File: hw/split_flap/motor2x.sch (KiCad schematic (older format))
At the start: 5 parts, among them J10 Conn_01x05, J9 Conn_01x05, U4 ULN2803A, U9 74HC595

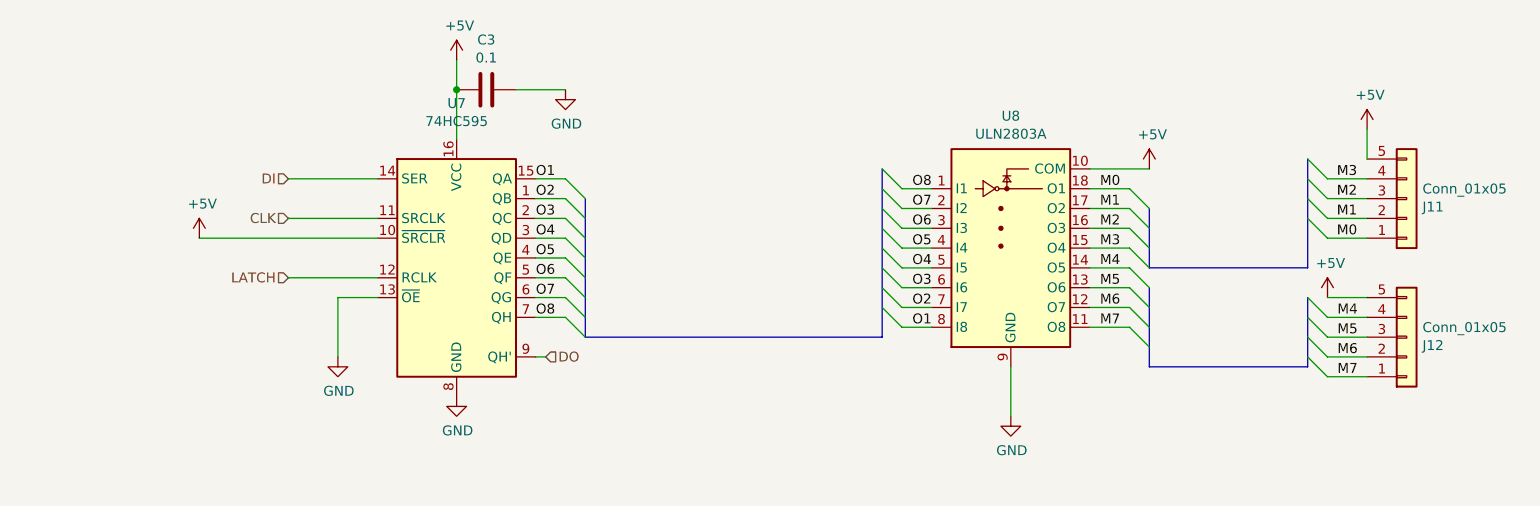
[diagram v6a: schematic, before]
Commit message: Add VCC for motors
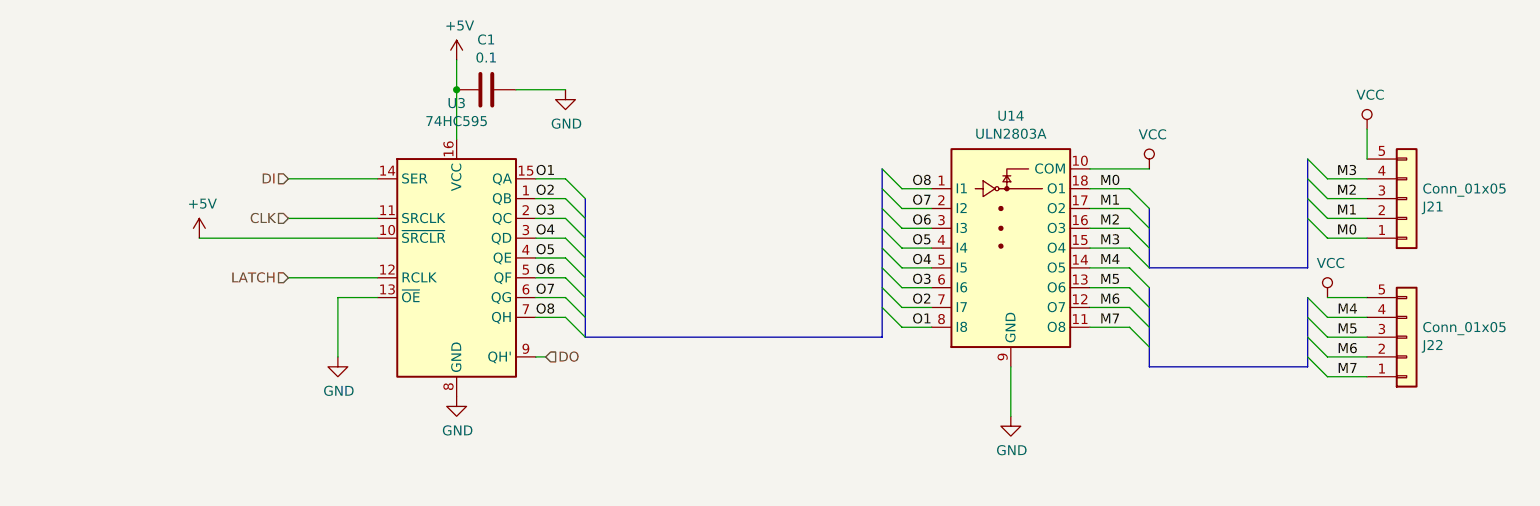
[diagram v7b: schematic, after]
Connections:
- net +5V: no longer J10.5 (Pin_5), J9.5 (Pin_5), U4.10 (COM)
- new net VCC: J10.5 (Pin_5), J9.5 (Pin_5), U4.10 (COM)
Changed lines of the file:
@@
 $Descr A4 11693 8268
 encoding utf-8
-Sheet 5 6
+Sheet 2 6
 Title ""
 Date ""
@@
 AR Path="/5E0964A4/5E0DEDAF" Ref="#PWR033"  Part="1"
 AR Path="/5E0B21A0/5E0DEDAF" Ref="#PWR051"  Part="1"
-F 0 "#PWR042" H 4850 3850 50  0001 C CNN
+F 0 "#PWR0159" H 4850 3850 50  0001 C CNN
 F 1 "GND" H 4855 3927 50  0000 C CNN
 F 2 "" H 4850 4100 50  0001 C CNN
@@
 AR Path="/5E0964A4/5DF98B62" Ref="#PWR032"  Part="1"
 AR Path="/5E0B21A0/5DF98B62" Ref="#PWR050"  Part="1"
-F 0 "#PWR041" H 4850 2250 50  0001 C CNN
+F 0 "#PWR012" H 4850 2250 50  0001 C CNN
 F 1 "+5V" H 4865 2573 50  0000 C CNN
 F 2 "" H 4850 2400 50  0001 C CNN
@@
 AR Path="/5E0964A4/5DF9B643" Ref="#PWR031"  Part="1"
 AR Path="/5E0B21A0/5DF9B643" Ref="#PWR049"  Part="1"
-F 0 "#PWR040" H 4250 3650 50  0001 C CNN
+F 0 "#PWR011" H 4250 3650 50  0001 C CNN
 F 1 "GND" H 4255 3727 50  0000 C CNN
 F 2 "" H 4250 3900 50  0001 C CNN
@@
 AR Path="/5E0964A4/5DF9D02C" Ref="#PWR030"  Part="1"
 AR Path="/5E0B21A0/5DF9D02C" Ref="#PWR048"  Part="1"
-F 0 "#PWR039" H 3550 3150 50  0001 C CNN
+F 0 "#PWR08" H 3550 3150 50  0001 C CNN
 F 1 "+5V" H 3565 3473 50  0000 C CNN
 F 2 "" H 3550 3300 50  0001 C CNN
@@
 AR Path="/5E092C79/5E0E710C" Ref="C3"  Part="1"
 AR Path="/5E0B21A0/5E0E710C" Ref="C4"  Part="1"
-F 0 "C3" V 5252 2550 50  0000 C CNN
+F 0 "C1" V 5252 2550 50  0000 C CNN
 F 1 "0.1" V 5161 2550 50  0000 C CNN
 F 2 "Capacitor_THT:C_Disc_D4.3mm_W1.9mm_P5.00mm" H 5038 2400 50  0001 C CNN
@@
 AR Path="/5E0964A4/5E0E7881" Ref="#PWR034"  Part="1"
 AR Path="/5E0B21A0/5E0E7881" Ref="#PWR052"  Part="1"
-F 0 "#PWR043" H 5400 2300 50  0001 C CNN
+F 0 "#PWR013" H 5400 2300 50  0001 C CNN
 F 1 "GND" H 5405 2377 50  0000 C CNN
 F 2 "" H 5400 2550 50  0001 C CNN
@@
 AR Path="/5E0964A4/5DF4397F" Ref="U5"  Part="1"
 AR Path="/5E092C79/5DF4397F" Ref="U7"  Part="1"
-F 0 "U7" H 4850 4181 50  0000 C CNN
+F 0 "U3" H 4850 4181 50  0000 C CNN
 F 1 "74HC595" H 4850 4090 50  0000 C CNN
 F 2 "Package_SO:SOP-16_4.55x10.3mm_P1.27mm" H 4850 3400 50  0001 C CNN
@@
 Wire Wire Line
 	5250 3700 5400 3700
-$Comp
-L power:+5V #PWR?
-U 1 1 5E0DED8E
-P 9250 3600
-AR Path="/5E0DED8E" Ref="#PWR?"  Part="1"
-AR Path="/5E0CA2EA/5E0DED8E" Ref="#PWR0122"  Part="1"
-AR Path="/5E1C4151/5E0DED8E" Ref="#PWR0128"  Part="1"
-AR Path="/5E1CE3D2/5E0DED8E" Ref="#PWR0134"  Part="1"
-AR Path="/5E1D4C2D/5E0DED8E" Ref="#PWR0140"  Part="1"
-AR Path="/5E2ED868/5E0DED8E" Ref="#PWR019"  Part="1"
-AR Path="/5DEBFEF8/5E0DED8E" Ref="#PWR0150"  Part="1"
-AR Path="/5DED9C19/5E0DED8E" Ref="#PWR0156"  Part="1"
-AR Path="/5DFFABAB/5E0DED8E" Ref="#PWR?"  Part="1"
-AR Path="/5DFFD987/5E0DED8E" Ref="#PWR?"  Part="1"
-AR Path="/5E08C84E/5E0DED8E" Ref="#PWR?"  Part="1"
-AR Path="/5E08C85A/5E0DED8E" Ref="#PWR?"  Part="1"
-AR Path="/5E092C79/5E0DED8E" Ref="#PWR047"  Part="1"
-AR Path="/5E0964A4/5E0DED8E" Ref="#PWR038"  Part="1"
-AR Path="/5E0B21A0/5E0DED8E" Ref="#PWR056"  Part="1"
-F 0 "#PWR047" H 9250 3450 50  0001 C CNN
-F 1 "+5V" H 9265 3773 50  0000 C CNN
-F 2 "" H 9250 3600 50  0001 C CNN
-F 3 "" H 9250 3600 50  0001 C CNN
-	1    9250 3600
-	1    0    0    -1
-$EndComp
 $Comp
 L Connector_Generic:Conn_01x05 J?
@@
 AR Path="/5E0964A4/5E0DED94" Ref="J10"  Part="1"
 AR Path="/5E0B21A0/5E0DED94" Ref="J14"  Part="1"
-F 0 "J12" H 9730 3842 50  0000 L CNN
+F 0 "J22" H 9730 3842 50  0000 L CNN
 F 1 "Conn_01x05" H 9730 3751 50  0000 L CNN
 F 2 "Connector_JST:JST_XH_B5B-XH-A_1x05_P2.50mm_Vertical" H 9650 3800 50  0001 C CNN
@@
 	1    9650 3800
 	1    0    0    1
-$EndComp
-Wire Wire Line
-	9450 2750 9450 2900
-$Comp
-L power:+5V #PWR?
-U 1 1 5E0DED9D
-P 9450 2750
-AR Path="/5E0DED9D" Ref="#PWR?"  Part="1"
-AR Path="/5E0CA2EA/5E0DED9D" Ref="#PWR0123"  Part="1"
-AR Path="/5E1C4151/5E0DED9D" Ref="#PWR0129"  Part="1"
-AR Path="/5E1CE3D2/5E0DED9D" Ref="#PWR0135"  Part="1"
-AR Path="/5E1D4C2D/5E0DED9D" Ref="#PWR0141"  Part="1"
-AR Path="/5E2ED868/5E0DED9D" Ref="#PWR018"  Part="1"
-AR Path="/5DEBFEF8/5E0DED9D" Ref="#PWR0151"  Part="1"
-AR Path="/5DED9C19/5E0DED9D" Ref="#PWR0157"  Part="1"
-AR Path="/5DFFABAB/5E0DED9D" Ref="#PWR?"  Part="1"
-AR Path="/5DFFD987/5E0DED9D" Ref="#PWR?"  Part="1"
-AR Path="/5E08C84E/5E0DED9D" Ref="#PWR?"  Part="1"
-AR Path="/5E08C85A/5E0DED9D" Ref="#PWR?"  Part="1"
-AR Path="/5E092C79/5E0DED9D" Ref="#PWR046"  Part="1"
-AR Path="/5E0964A4/5E0DED9D" Ref="#PWR037"  Part="1"
-AR Path="/5E0B21A0/5E0DED9D" Ref="#PWR055"  Part="1"
-F 0 "#PWR046" H 9450 2600 50  0001 C CNN
-F 1 "+5V" H 9465 2923 50  0000 C CNN
-F 2 "" H 9450 2750 50  0001 C CNN
-F 3 "" H 9450 2750 50  0001 C CNN
-	1    9450 2750
-	1    0    0    -1
-$EndComp
-$Comp
-L power:+5V #PWR?
-U 1 1 5E0DEDA9
-P 8350 2950
-AR Path="/5E0DEDA9" Ref="#PWR?"  Part="1"
-AR Path="/5E0CA2EA/5E0DEDA9" Ref="#PWR0125"  Part="1"
-AR Path="/5E1C4151/5E0DEDA9" Ref="#PWR0131"  Part="1"
-AR Path="/5E1CE3D2/5E0DEDA9" Ref="#PWR0137"  Part="1"
-AR Path="/5E1D4C2D/5E0DEDA9" Ref="#PWR0143"  Part="1"
-AR Path="/5E2ED868/5E0DEDA9" Ref="#PWR017"  Part="1"
-AR Path="/5DEBFEF8/5E0DEDA9" Ref="#PWR0152"  Part="1"
-AR Path="/5DED9C19/5E0DEDA9" Ref="#PWR0158"  Part="1"
-AR Path="/5DFFABAB/5E0DEDA9" Ref="#PWR?"  Part="1"
-AR Path="/5DFFD987/5E0DEDA9" Ref="#PWR?"  Part="1"
-AR Path="/5E08C84E/5E0DEDA9" Ref="#PWR?"  Part="1"
-AR Path="/5E08C85A/5E0DEDA9" Ref="#PWR?"  Part="1"
-AR Path="/5E092C79/5E0DEDA9" Ref="#PWR045"  Part="1"
-AR Path="/5E0964A4/5E0DEDA9" Ref="#PWR036"  Part="1"
-AR Path="/5E0B21A0/5E0DEDA9" Ref="#PWR054"  Part="1"
-F 0 "#PWR045" H 8350 2800 50  0001 C CNN
-F 1 "+5V" H 8365 3123 50  0000 C CNN
-F 2 "" H 8350 2950 50  0001 C CNN
-F 3 "" H 8350 2950 50  0001 C CNN
-	1    8350 2950
-	1    0    0    -1
 $EndComp
 $Comp
@@
 AR Path="/5E0964A4/5E0DEDB5" Ref="#PWR035"  Part="1"
 AR Path="/5E0B21A0/5E0DEDB5" Ref="#PWR053"  Part="1"
-F 0 "#PWR044" H 7650 3950 50  0001 C CNN
+F 0 "#PWR0160" H 7650 3950 50  0001 C CNN
 F 1 "GND" H 7655 4027 50  0000 C CNN
 F 2 "" H 7650 4200 50  0001 C CNN
@@
 AR Path="/5E0964A4/5E0DEDBB" Ref="J9"  Part="1"
 AR Path="/5E0B21A0/5E0DEDBB" Ref="J13"  Part="1"
-F 0 "J11" H 9730 3142 50  0000 L CNN
+F 0 "J21" H 9730 3142 50  0000 L CNN
 F 1 "Conn_01x05" H 9730 3051 50  0000 L CNN
 F 2 "Connector_JST:JST_XH_B5B-XH-A_1x05_P2.50mm_Vertical" H 9650 3100 50  0001 C CNN
@@
 AR Path="/5E0964A4/5E0DEDCB" Ref="U6"  Part="1"
 AR Path="/5E0B21A0/5E0DEDCB" Ref="U10"  Part="1"
-F 0 "U8" H 7650 3817 50  0000 C CNN
+F 0 "U14" H 7650 3817 50  0000 C CNN
 F 1 "ULN2803A" H 7650 3726 50  0000 C CNN
 F 2 "Package_SO:SOP-18_7x12.5mm_P1.27mm" H 7700 2600 50  0001 L CNN
@@
 Wire Bus Line
 	8350 3450 9150 3450
+$Comp
+L power:VCC #PWR055
+U 1 1 5DF9DFD8
+P 8350 2950
+AR Path="/5E092C79/5DF9DFD8" Ref="#PWR055"  Part="1"
+AR Path="/5DED9C19/5DF9DFD8" Ref="#PWR045"  Part="1"
+AR Path="/5E0964A4/5DF9DFD8" Ref="#PWR047"  Part="1"
+AR Path="/5E0B21A0/5DF9DFD8" Ref="#PWR057"  Part="1"
+F 0 "#PWR045" H 8350 2800 50  0001 C CNN
+F 1 "VCC" H 8367 3123 50  0000 C CNN
+F 2 "" H 8350 2950 50  0001 C CNN
+F 3 "" H 8350 2950 50  0001 C CNN
+	1    8350 2950
+	1    0    0    -1
+$EndComp
+Wire Wire Line
+	9450 2750 9450 2900
+$Comp
+L power:VCC #PWR056
+U 1 1 5DF9E5BE
+P 9450 2750
+AR Path="/5E092C79/5DF9E5BE" Ref="#PWR056"  Part="1"
+AR Path="/5DED9C19/5DF9E5BE" Ref="#PWR046"  Part="1"
+AR Path="/5E0964A4/5DF9E5BE" Ref="#PWR054"  Part="1"
+AR Path="/5E0B21A0/5DF9E5BE" Ref="#PWR058"  Part="1"
+F 0 "#PWR046" H 9450 2600 50  0001 C CNN
+F 1 "VCC" H 9467 2923 50  0000 C CNN
+F 2 "" H 9450 2750 50  0001 C CNN
+F 3 "" H 9450 2750 50  0001 C CNN
+	1    9450 2750
+	1    0    0    -1
+$EndComp
+$Comp
+L power:VCC #PWR069
+U 1 1 5DFA3442
+P 9250 3600
+AR Path="/5E092C79/5DFA3442" Ref="#PWR069"  Part="1"
+AR Path="/5DED9C19/5DFA3442" Ref="#PWR059"  Part="1"
+AR Path="/5E0964A4/5DFA3442" Ref="#PWR068"  Part="1"
+AR Path="/5E0B21A0/5DFA3442" Ref="#PWR070"  Part="1"
+F 0 "#PWR059" H 9250 3450 50  0001 C CNN
+F 1 "VCC" H 9267 3773 50  0000 C CNN
+F 2 "" H 9250 3600 50  0001 C CNN
+F 3 "" H 9250 3600 50  0001 C CNN
+	1    9250 3600
+	1    0    0    -1
+$EndComp
 Wire Bus Line
 	8350 3150 8350 3450

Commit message: Add mounting holes, logo and capacitor for +5V
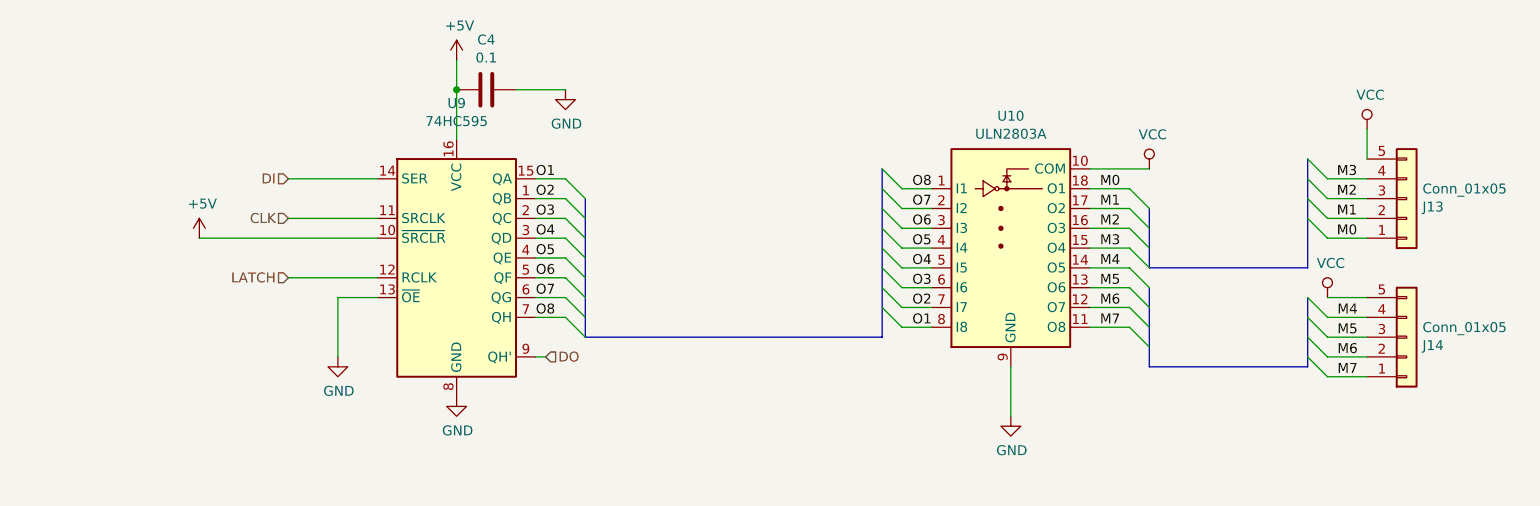
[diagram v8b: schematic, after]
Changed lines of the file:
@@
 AR Path="/5E0964A4/5E0DEDAF" Ref="#PWR033"  Part="1"
 AR Path="/5E0B21A0/5E0DEDAF" Ref="#PWR051"  Part="1"
-F 0 "#PWR0159" H 4850 3850 50  0001 C CNN
+F 0 "#PWR051" H 4850 3850 50  0001 C CNN
 F 1 "GND" H 4855 3927 50  0000 C CNN
 F 2 "" H 4850 4100 50  0001 C CNN
@@
 AR Path="/5E0964A4/5DF98B62" Ref="#PWR032"  Part="1"
 AR Path="/5E0B21A0/5DF98B62" Ref="#PWR050"  Part="1"
-F 0 "#PWR012" H 4850 2250 50  0001 C CNN
+F 0 "#PWR050" H 4850 2250 50  0001 C CNN
 F 1 "+5V" H 4865 2573 50  0000 C CNN
 F 2 "" H 4850 2400 50  0001 C CNN
@@
 AR Path="/5E0964A4/5DF9B643" Ref="#PWR031"  Part="1"
 AR Path="/5E0B21A0/5DF9B643" Ref="#PWR049"  Part="1"
-F 0 "#PWR011" H 4250 3650 50  0001 C CNN
+F 0 "#PWR049" H 4250 3650 50  0001 C CNN
 F 1 "GND" H 4255 3727 50  0000 C CNN
 F 2 "" H 4250 3900 50  0001 C CNN
@@
 AR Path="/5E0964A4/5DF9D02C" Ref="#PWR030"  Part="1"
 AR Path="/5E0B21A0/5DF9D02C" Ref="#PWR048"  Part="1"
-F 0 "#PWR08" H 3550 3150 50  0001 C CNN
+F 0 "#PWR048" H 3550 3150 50  0001 C CNN
 F 1 "+5V" H 3565 3473 50  0000 C CNN
 F 2 "" H 3550 3300 50  0001 C CNN
@@
 AR Path="/5E092C79/5E0E710C" Ref="C3"  Part="1"
 AR Path="/5E0B21A0/5E0E710C" Ref="C4"  Part="1"
-F 0 "C1" V 5252 2550 50  0000 C CNN
+F 0 "C4" V 5252 2550 50  0000 C CNN
 F 1 "0.1" V 5161 2550 50  0000 C CNN
 F 2 "Capacitor_THT:C_Disc_D4.3mm_W1.9mm_P5.00mm" H 5038 2400 50  0001 C CNN
@@
 AR Path="/5E0964A4/5E0E7881" Ref="#PWR034"  Part="1"
 AR Path="/5E0B21A0/5E0E7881" Ref="#PWR052"  Part="1"
-F 0 "#PWR013" H 5400 2300 50  0001 C CNN
+F 0 "#PWR052" H 5400 2300 50  0001 C CNN
 F 1 "GND" H 5405 2377 50  0000 C CNN
 F 2 "" H 5400 2550 50  0001 C CNN
@@
 AR Path="/5E0964A4/5DF4397F" Ref="U5"  Part="1"
 AR Path="/5E092C79/5DF4397F" Ref="U7"  Part="1"
-F 0 "U3" H 4850 4181 50  0000 C CNN
+F 0 "U9" H 4850 4181 50  0000 C CNN
 F 1 "74HC595" H 4850 4090 50  0000 C CNN
 F 2 "Package_SO:SOP-16_4.55x10.3mm_P1.27mm" H 4850 3400 50  0001 C CNN
@@
 AR Path="/5E0964A4/5E0DED94" Ref="J10"  Part="1"
 AR Path="/5E0B21A0/5E0DED94" Ref="J14"  Part="1"
-F 0 "J22" H 9730 3842 50  0000 L CNN
+F 0 "J14" H 9730 3842 50  0000 L CNN
 F 1 "Conn_01x05" H 9730 3751 50  0000 L CNN
 F 2 "Connector_JST:JST_XH_B5B-XH-A_1x05_P2.50mm_Vertical" H 9650 3800 50  0001 C CNN
@@
 AR Path="/5E0964A4/5E0DEDB5" Ref="#PWR035"  Part="1"
 AR Path="/5E0B21A0/5E0DEDB5" Ref="#PWR053"  Part="1"
-F 0 "#PWR0160" H 7650 3950 50  0001 C CNN
+F 0 "#PWR053" H 7650 3950 50  0001 C CNN
 F 1 "GND" H 7655 4027 50  0000 C CNN
 F 2 "" H 7650 4200 50  0001 C CNN
@@
 AR Path="/5E0964A4/5E0DEDBB" Ref="J9"  Part="1"
 AR Path="/5E0B21A0/5E0DEDBB" Ref="J13"  Part="1"
-F 0 "J21" H 9730 3142 50  0000 L CNN
+F 0 "J13" H 9730 3142 50  0000 L CNN
 F 1 "Conn_01x05" H 9730 3051 50  0000 L CNN
 F 2 "Connector_JST:JST_XH_B5B-XH-A_1x05_P2.50mm_Vertical" H 9650 3100 50  0001 C CNN
@@
 AR Path="/5E0964A4/5E0DEDCB" Ref="U6"  Part="1"
 AR Path="/5E0B21A0/5E0DEDCB" Ref="U10"  Part="1"
-F 0 "U14" H 7650 3817 50  0000 C CNN
+F 0 "U10" H 7650 3817 50  0000 C CNN
 F 1 "ULN2803A" H 7650 3726 50  0000 C CNN
 F 2 "Package_SO:SOP-18_7x12.5mm_P1.27mm" H 7700 2600 50  0001 L CNN
@@
 AR Path="/5E0964A4/5DF9DFD8" Ref="#PWR047"  Part="1"
 AR Path="/5E0B21A0/5DF9DFD8" Ref="#PWR057"  Part="1"
-F 0 "#PWR045" H 8350 2800 50  0001 C CNN
+F 0 "#PWR057" H 8350 2800 50  0001 C CNN
 F 1 "VCC" H 8367 3123 50  0000 C CNN
 F 2 "" H 8350 2950 50  0001 C CNN
@@
 AR Path="/5E0964A4/5DF9E5BE" Ref="#PWR054"  Part="1"
 AR Path="/5E0B21A0/5DF9E5BE" Ref="#PWR058"  Part="1"
-F 0 "#PWR046" H 9450 2600 50  0001 C CNN
+F 0 "#PWR058" H 9450 2600 50  0001 C CNN
 F 1 "VCC" H 9467 2923 50  0000 C CNN
 F 2 "" H 9450 2750 50  0001 C CNN
@@
 AR Path="/5E0964A4/5DFA3442" Ref="#PWR068"  Part="1"
 AR Path="/5E0B21A0/5DFA3442" Ref="#PWR070"  Part="1"
-F 0 "#PWR059" H 9250 3450 50  0001 C CNN
+F 0 "#PWR070" H 9250 3450 50  0001 C CNN
 F 1 "VCC" H 9267 3773 50  0000 C CNN
 F 2 "" H 9250 3600 50  0001 C CNN
